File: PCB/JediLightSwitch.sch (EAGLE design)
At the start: 24 parts, among them U1 APDS-9960, U2 HTU21DSMD, U3 PHOTON_SMD, U4 AT42QT1010SOT23

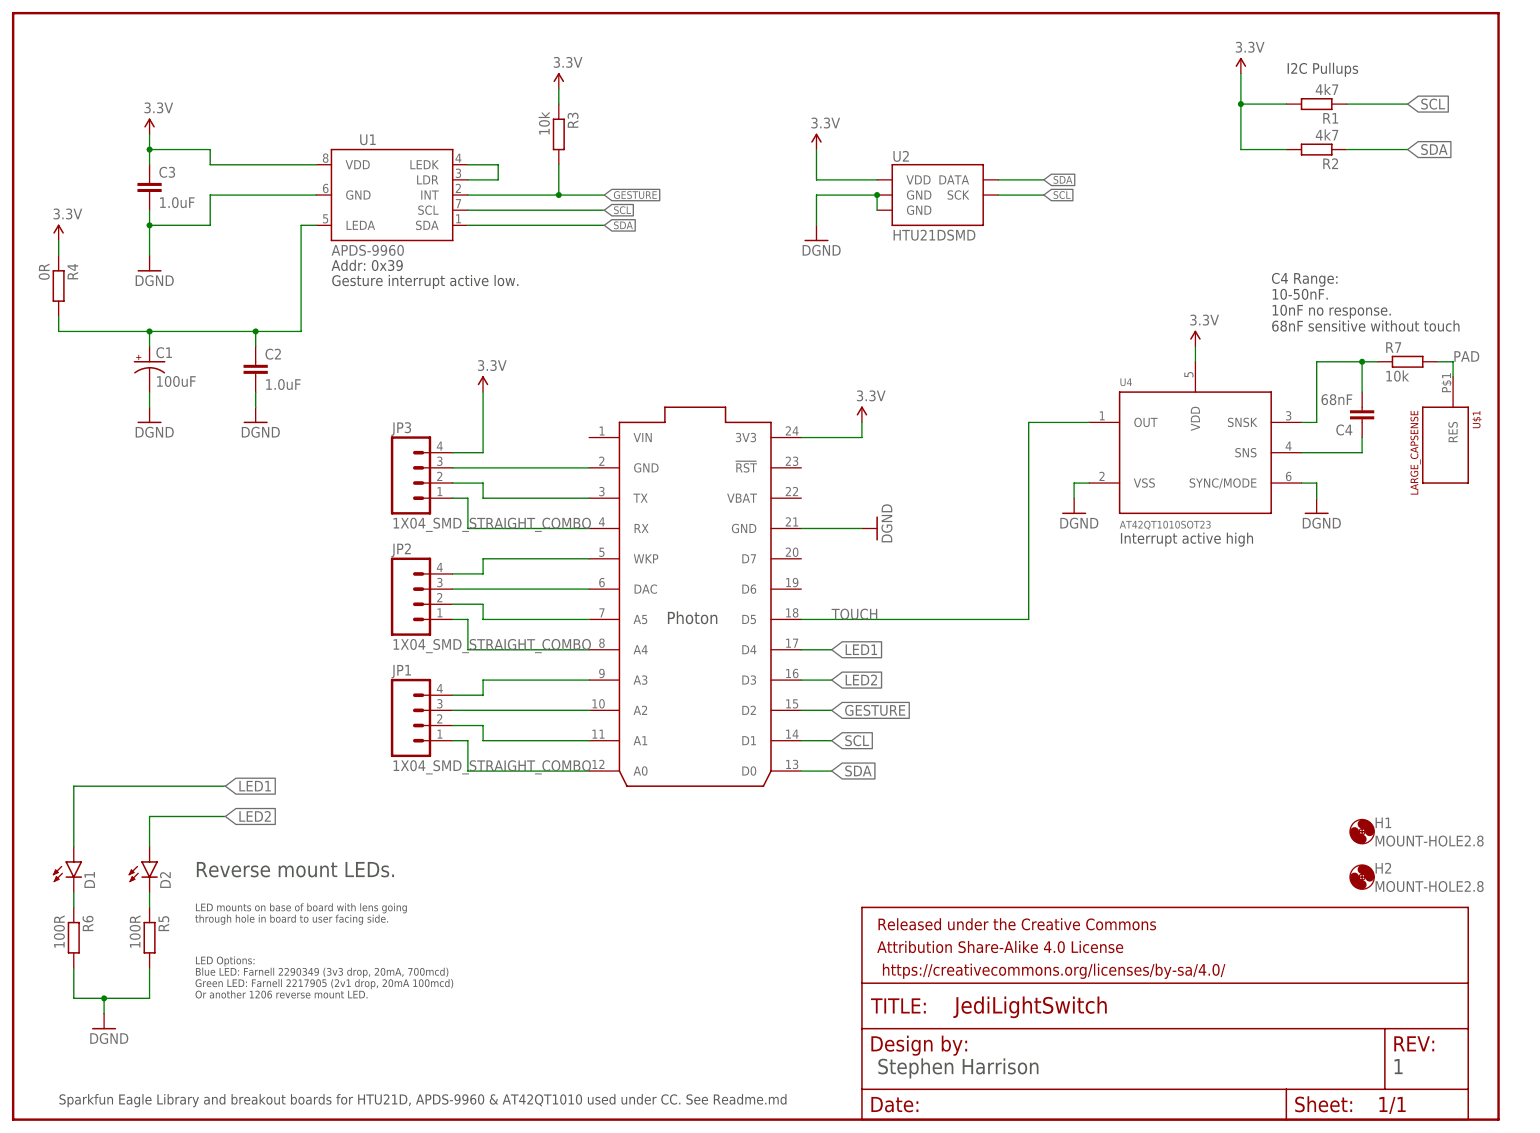
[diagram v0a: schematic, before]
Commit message: Updated Schematic & PCB: * Added 2x extra LEDs for bottom left/right. * Added second capacitor and resistor options to cap sense circuit. * Cap sense chip is now powered by Photon to allow for re-calibration by power cycle. * Added ground planes for top and bottom of PCB. * Moved some parts in (e.g. resistors for leds and I2C pull-ups) to reduce hit area on enclosure. * Added mode daughter board connectors * Tidied up
Bumped revision of cicuit/board to V1.1
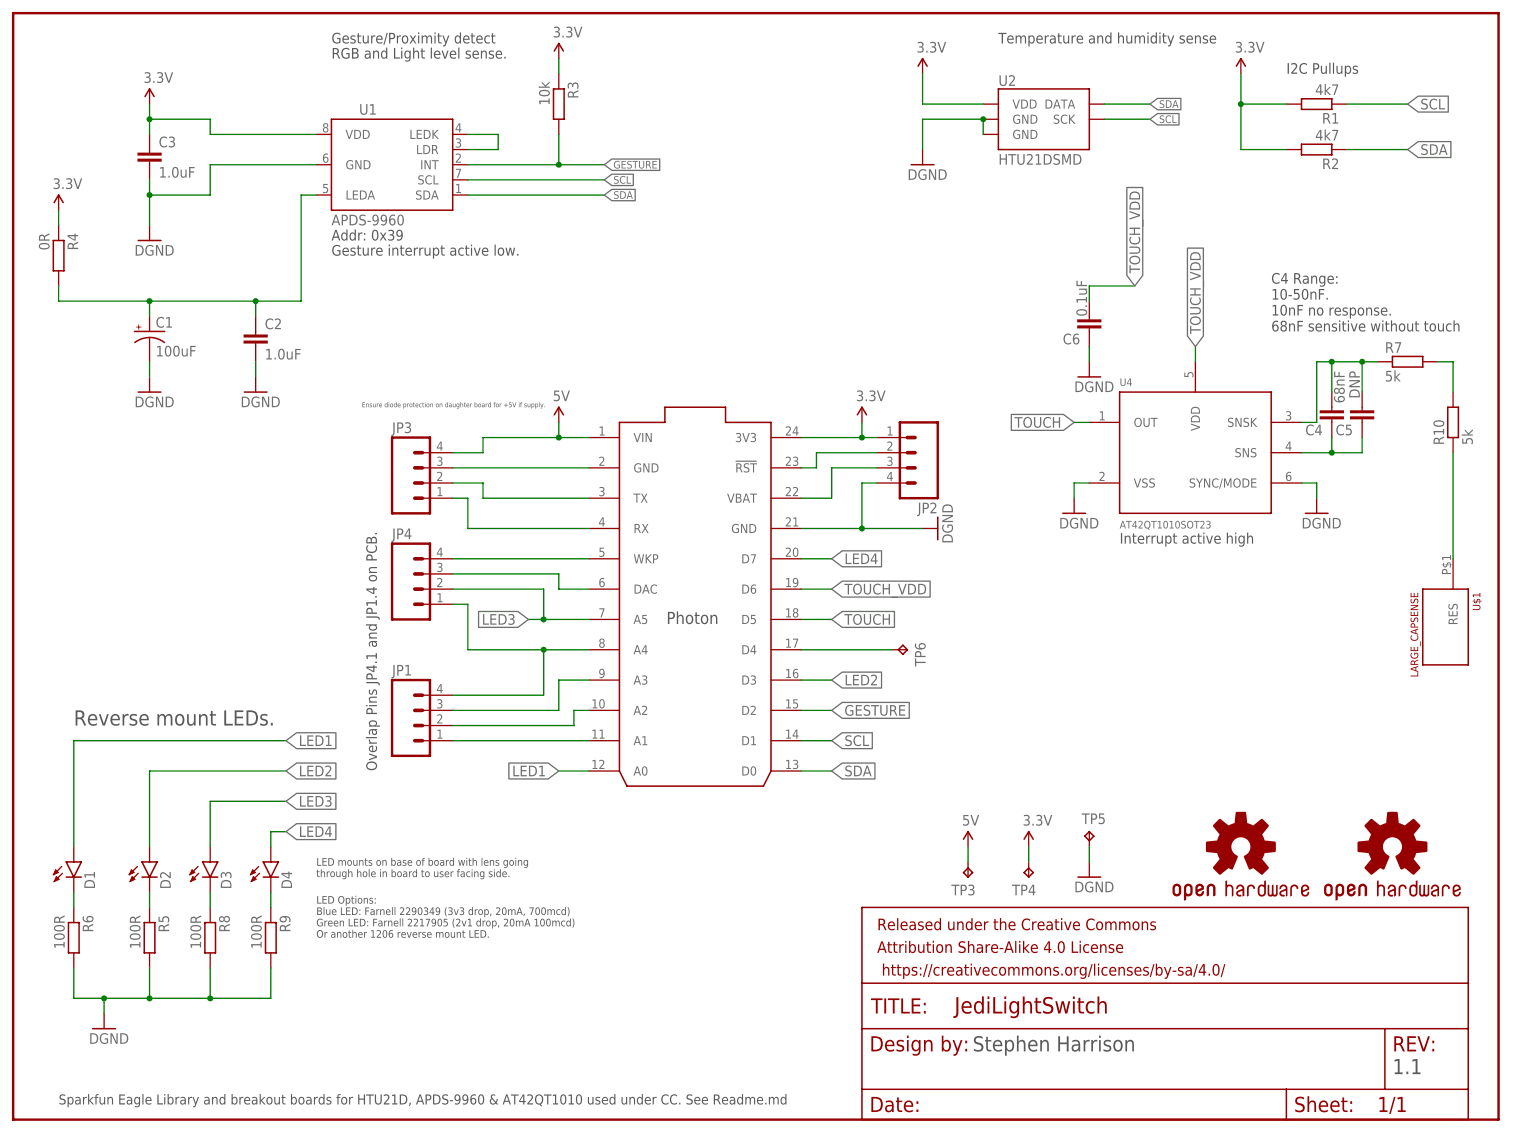
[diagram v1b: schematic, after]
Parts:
- removed H1, H2: MOUNT-HOLE2.8, holes:MOUNT-HOLE2.8
- added C5: DNP, rcl:C-EUC0805
- added C6: 0.1uF, rcl:C-EUC0805
- added D3, D4: (no value), SparkFun-LED:LED1206-BOTTOM
- added JP4: (no value), SparkFun-Connectors:M04SMD_STRAIGHT_COMBO
- added LOGO1, LOGO2: OSHW-LOGOM, SparkFun-Aesthetics:OSHW-LOGOM
- added R10: 5k, rcl:R-EU_R0805
- added R8, R9: 100R, rcl:R-EU_R0805
- added TP3, TP5, TP6: TPTP20R, testpad:TPTP20R
- added TP4: 3v3, testpad:TPTP20R
- JP1, JP2, JP3: value 1X04_SMD_STRAIGHT_COMBO -> (none)
- R7: value 10k -> 5k
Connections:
- removed net PAD: R7.2, U$1.RES
- new net 5V: JP3.4, TP3.TP, U3G$1.VIN
- new net LED3: D3.A, JP4.2, U3G$1.A5
- new net LED4: D4.A, U3G$1.D7
- new net N$11: JP1.2, U3G$1.A2
- new net N$16: JP4.3, U3G$1.DAC
- new net N$22: TP6.TP, U3G$1.D4
- new net N$30: D3.C, R8.1
- new net N$31: D4.C, R9.1
- new net TOUCH_VDD: C6.2, U3G$1.D6, U4.VDD
- net 3.3V: now also JP2.1, TP4.TP; no longer JP3.4, U4.VDD
- net GND: now also C6.1, JP2.4, R8.2, R9.2, TP5.TP
- net LED1: now also U3G$1.A0; no longer U3G$1.D4
- net N$10: now also JP4.4, U3G$1.WKP; no longer JP2.2, U3G$1.A5
- net N$12: now also JP1.3, U3G$1.A3; no longer JP2.3, U3G$1.DAC
- net N$13: now also JP1.4, JP4.1, U3G$1.A4; no longer JP2.4, U3G$1.WKP
- net N$19: now also C5.2
- net N$20: now also C5.1
- net N$5: now also JP2.2, U3G$1.!RST; no longer JP1.1, U3G$1.A0
- net N$6: now also JP1.1; no longer JP1.2
- net N$7: now also JP2.3, U3G$1.VBAT; no longer JP1.3, U3G$1.A2
- net N$8: now also R10.2, R7.2; no longer JP1.4, U3G$1.A3
- net N$9: now also R10.1, U$1.RES; no longer JP2.1, U3G$1.A4
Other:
- note added: "1.1"
- note added: "Ensure diode protection on daughter board for +5V if supply."
- note added: "Gesture/Proximity detect"
- note added: "Overlap Pins JP4.1 and JP1.4 on PCB."
- note added: "RGB and Light level sense."
- note added: "Temperature and humidity sense"
- note removed: "1"
- moved on the sheet: C1, C2, C3, C4, JP2, R3, R4, U$1, U1, U2

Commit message: Version 1.2 of Jedi Light Switch as sent to OSH Park.
Added:
* 4x back facing NeoPixes.
* LiPol interface. Charger and monitor.
* 2x IR LEDs
* TEMT6000 light sensor as gesture sensor is very direct


Re-arranged board top so that all the sensors are in a single row.

Moved touch panel up very slightly

Reduced add-on board connectors to 2, one either side of Photon.
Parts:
- removed JP1, JP4: (no value), SparkFun-Connectors:M04SMD_STRAIGHT_COMBO
- added C10, C7, C8, C9: 0.1uF, rcl:C-EUC0805
- added C11, C12: 4.7uF, rcl:C-EUC0805
- added C13, C14: 1.0uF, rcl:C-EUC0805
- added D5, D6, D7, D8: WS2812B, SparkFun-LED:WS2812B
- added D9: MBRA140, SparkFun-DiscreteSemi:MBRA140
- added FRAME1: FRAME-LETTERNO_PACKAGE, SparkFun-Aesthetics:FRAME-LETTERNO_PACKAGE
- added J1: (no value), SparkFun-Connectors:JST_2MM_MALE
- added LED1, LED2: IR, led:LEDSMT1206
- added Q1: MOSFET-NCHANNELAO3404A, SparkFun-DiscreteSemi:MOSFET-NCHANNELAO3404A
- added R11: 470, rcl:R-EU_R0805
- added R12: DNP, rcl:R-EU_R0805
- added R13, R14: 100k, rcl:R-EU_R0805
- added R15, R16, R19: 10k, rcl:R-EU_R0805
- added R17: 2k, rcl:R-EU_R0805
- added R18: 10R, rcl:R-EU_R0805
- added R20, R21: 60R, rcl:R-EU_R0805
- added R22, R23: 1k, rcl:R-EU_R0805
- added TP1, TP2, TP7, TP8, TP9: TPTP20R, testpad:TPTP20R
- added U5: TEMT6000, SparkFun-Sensors:LIGHTSENSORTEMT6000
- added U6: MCP73831, SparkFun-PowerIC:MCP73831
- added U7: MAX1704X, SparkFun-PowerIC:MAX1704X
- C4: value 68nF -> 22nF
- R5, R6, R8, R9: value 100R -> 1k
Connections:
- removed net N$10: JP4.4, U3G$1.WKP
- new net ALERT: U7.ALT
- new net BATT_MON: R13.2, R14.1, U3G$1.A4
- new net CHARGE_STAT: R16.1, U3G$1.A3, U6.STAT
- new net D4: TP8.TP, U3G$1.D4
- new net DAC: TP6.TP, U3G$1.DAC
- new net IRLED_DRIVE: R18.2, U3G$1.A0
- new net LIGHT_LEVEL: R15.1, U3G$1.A1, U5.E1
- new net N$17: D5.DOUT, TP1.TP
- new net N$18: D6.DIN, D7.DOUT
- new net N$21: D5.DIN, D6.DOUT
- new net N$23: LED2.A, R21.1
- new net N$24: LED1.C, LED2.C, Q1.D
- new net N$25: R22.1, U7.QST
- new net NEOPIXELS_DIN: R11.1, R12.2, U3G$1.WKP
- new net V_BATT: C11.1, D9.A, J1.+, R13.1, R23.1, TP2.TP, U6.VBAT
- net 3.3V: now also C14.1, R16.2, U5.C1, U7.VDD
- net 5V: now also C10.1, C12.2, C13.1, C7.1, C8.1, C9.1, D5.VDD, D6.VDD, D7.VDD, D8.VDD, D9.C, R12.1, R20.2, R21.2, U6.VIN
- net GND: now also C10.2, C11.2, C12.1, C13.2, C14.2, C7.2, C8.2, C9.2, D5.VSS, D6.VSS, D7.VSS, D8.VSS, J1.-, Q1.S, R14.2, R15.2, R17.1, R19.1, R22.2, TP9.TP, U6.VSS, U7.CTG, U7.GND@4, U7.GND@EP
- net LED1: now also U3G$1.A2; no longer U3G$1.A0
- net LED3: no longer JP4.2
- net N$11: now also R17.2, U6.PROG; no longer JP1.2, U3G$1.A2
- net N$12: now also LED1.A, R20.1; no longer JP1.3, U3G$1.A3
- net N$13: now also D7.DIN, D8.DOUT; no longer JP1.4, JP4.1, U3G$1.A4
- net N$16: now also R23.2, U7.CELL; no longer JP4.3, U3G$1.DAC
- net N$22: now also D8.DIN, R11.2; no longer TP6.TP, U3G$1.D4
- net N$6: now also Q1.G, R18.1, R19.2; no longer JP1.1, U3G$1.A1
- net SCL: now also U7.SCL
- net SDA: now also U7.SDA
- net TOUCH_VDD: now also TP7.TP
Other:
- note added: "1.2"
- note added: "5v Pullup to Help Din if needed."
- note added: "A3 & DAC not 5V Tol."
- note added: "Bottom Left"
- note added: "Bottom Right"
- note added: "LiPol Battery Charger"
- note added: "Neopixels need DIN to be >70% of VDD."
- note added: "Reserved: Buzzer"
- note added: "Reserved: Second touch pad."
- note added: "Top Left"
- note added: "Top Right"
- note added: "Using 4.5V power from Photon VIN pin 3v3 == 73% which should be enough to drive the pixels."
- note removed: "1.1"
- note removed: "Overlap Pins JP4.1 and JP1.4 on PCB."

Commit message: Updated resistor values.
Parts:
- R10, R7: value 5k -> 4k7
- R20, R21: value 60R -> 62R
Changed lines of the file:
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@@
 <setting verticaltext="up"/>
 </settings>
-<grid distance="0.1" unitdist="inch" unit="inch" style="lines" multiple="1" display="yes" altdistance="0.01" altunitdist="inch" altunit="inch"/>
+<grid distance="0.1" unitdist="inch" unit="inch" style="lines" multiple="1" display="no" altdistance="0.01" altunitdist="inch" altunit="inch"/>
 <layers>
 <layer number="1" name="Top" color="4" fill="1" visible="no" active="no"/>
@@
 <part name="GND6" library="SparkFun-Aesthetics" deviceset="DGND" device=""/>
 <part name="U4" library="SparkFun-DigitalIC" deviceset="AT42QT1010" device="SOT23"/>
-<part name="R7" library="rcl" deviceset="R-EU_" device="R0805" value="5k"/>
+<part name="R7" library="rcl" deviceset="R-EU_" device="R0805" value="4k7"/>
 <part name="GND7" library="SparkFun-Aesthetics" deviceset="DGND" device=""/>
 <part name="GND8" library="SparkFun-Aesthetics" deviceset="DGND" device=""/>
@@
 <part name="JP2" library="SparkFun-Connectors" deviceset="M04" device="SMD_STRAIGHT_COMBO"/>
 <part name="LOGO1" library="SparkFun-Aesthetics" deviceset="OSHW-LOGO" device="M"/>
-<part name="R10" library="rcl" deviceset="R-EU_" device="R0805" value="5k"/>
+<part name="R10" library="rcl" deviceset="R-EU_" device="R0805" value="4k7"/>
 <part name="C6" library="rcl" deviceset="C-EU" device="C0805" value="0.1uF"/>
 <part name="GND17" library="SparkFun-Aesthetics" deviceset="DGND" device=""/>
@@
 <part name="LED1" library="led" deviceset="LED" device="SMT1206" value="IR"/>
 <part name="LED2" library="led" deviceset="LED" device="SMT1206" value="IR"/>
-<part name="R20" library="rcl" deviceset="R-EU_" device="R0805" value="60R"/>
-<part name="R21" library="rcl" deviceset="R-EU_" device="R0805" value="60R"/>
+<part name="R20" library="rcl" deviceset="R-EU_" device="R0805" value="62R"/>
+<part name="R21" library="rcl" deviceset="R-EU_" device="R0805" value="62R"/>
 <part name="C13" library="rcl" deviceset="C-EU" device="C0805" value="1.0uF"/>
 <part name="GND28" library="SparkFun-Aesthetics" deviceset="DGND" device=""/>
